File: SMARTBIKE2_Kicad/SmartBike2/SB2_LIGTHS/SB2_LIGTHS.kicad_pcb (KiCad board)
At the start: 2 copper layers, 45 x 45 mm, 34 parts, among them J1 Conn_01x02, J2 RJ45, Q1 SI2302, Q2 FDN340P, Q3 SI2302, Q4 SI2302, Q5 SI2302, U1 NA555D, U2 LM358

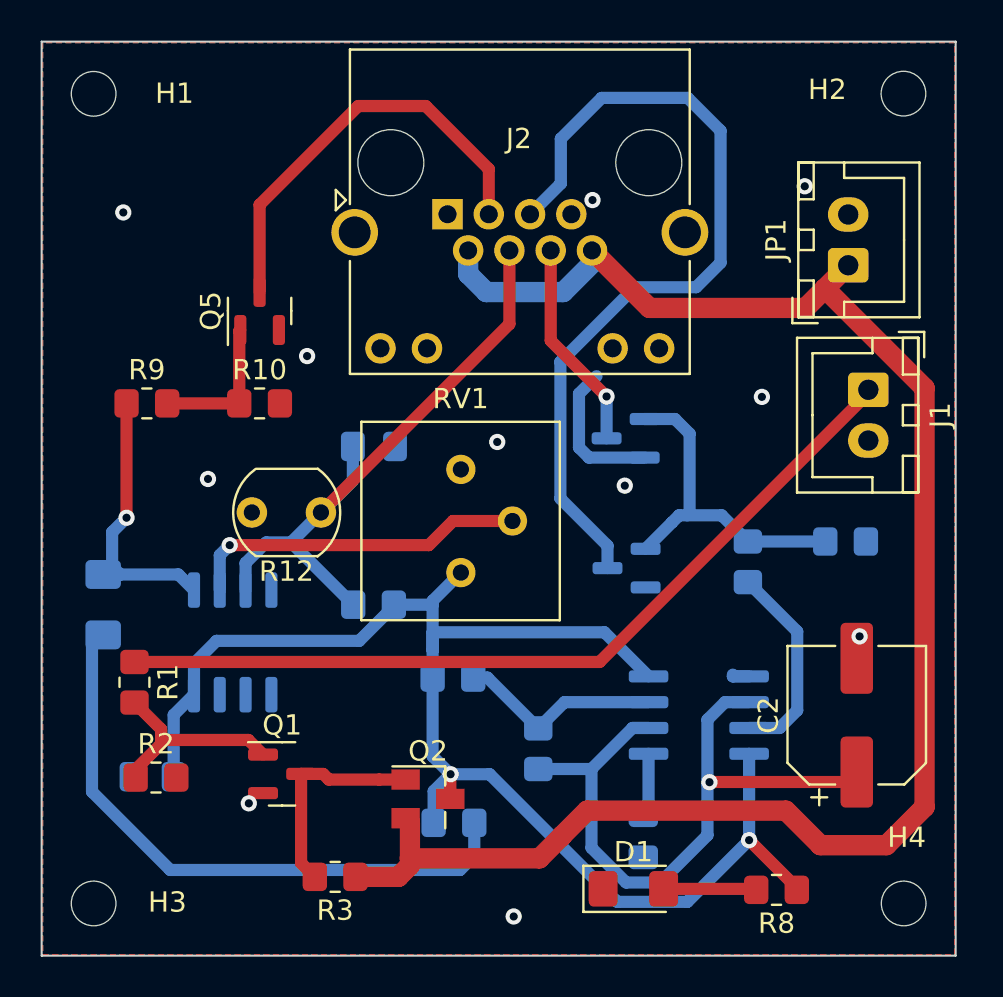
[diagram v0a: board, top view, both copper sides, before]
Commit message: Impresión vías sin metalización
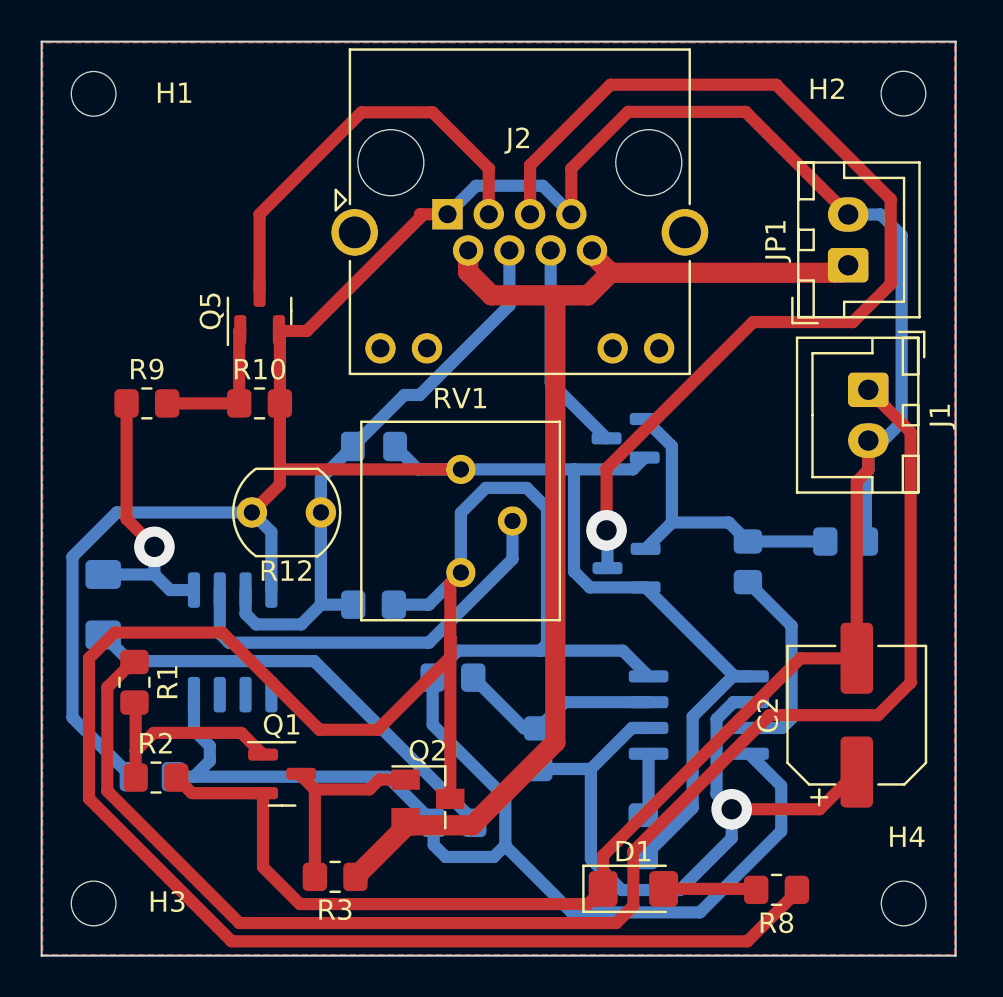
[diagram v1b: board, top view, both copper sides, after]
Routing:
- net GND: track 8.32 -> 195.9 mm, vias 11 -> 0
- net /+VL: track 72.5 -> 165.2 mm, vias 2 -> 0
- net /CtrLuces: track 41.8 -> 71.0 mm
- net +5V: track 84.2 -> 57.3 mm
- net /Direccionales/VDD_der: track 41.2 -> 51.0 mm, vias 0 -> 1
- net Net-(D2-A): track 30.3 -> 22.2 mm
- net Net-(U2A--): track 16.8 -> 20.3 mm, vias 1 -> 0
- net /Luz Frontal/Vswf: track 31.1 -> 28.8 mm
- net /Direccionales/TRIG: track 33.2 -> 34.4 mm
- net /Direccionales/Vosc: track 16.6 -> 15.4 mm
- net Net-(Q1-Pad1): track 10.1 -> 10.8 mm
- net Net-(Q2-G): track 10.6 -> 10.0 mm
- net /Luz Frontal/VDD_FRONT: track 21.1 -> 20.6 mm
- net /Direccionales/VDD_izq: vias 1 -> 0
